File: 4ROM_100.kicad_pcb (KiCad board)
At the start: 2 copper layers, 38 x 16.6 mm, 7 parts, among them J1 Tandy_100_102_200_option_rom, J2 4ROM_prog_female, U1 SST39SF010A

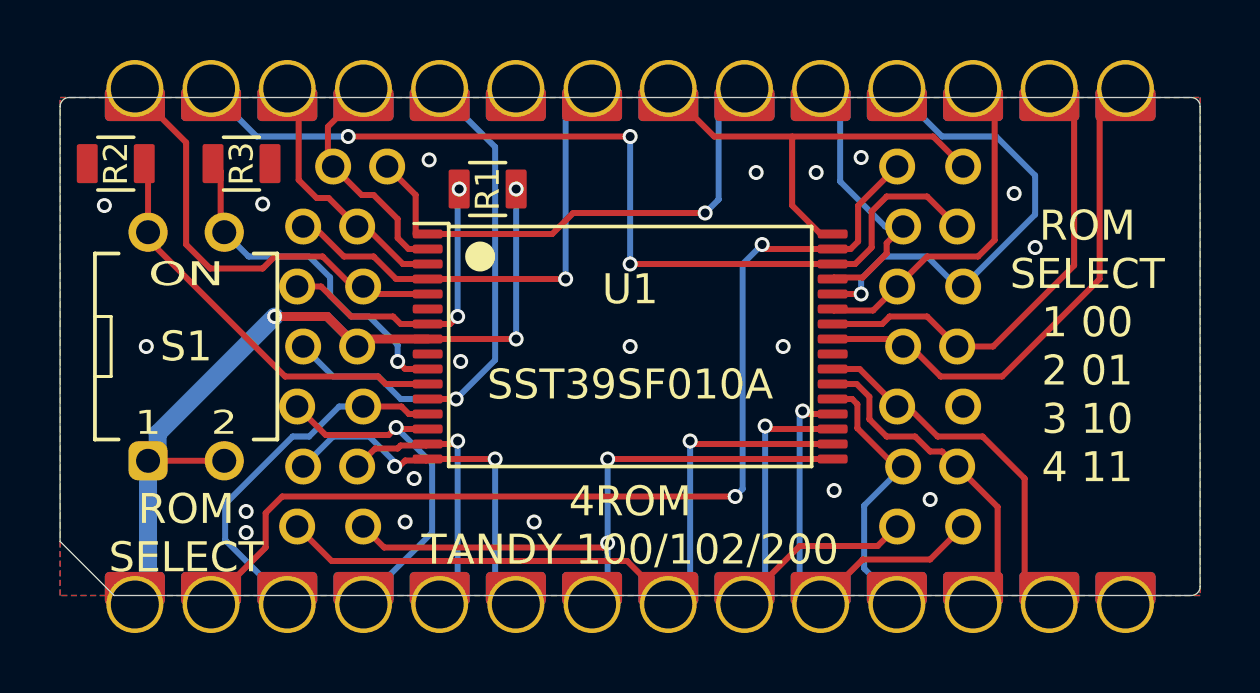
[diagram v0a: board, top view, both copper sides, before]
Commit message: 4ROM_78802 and programming adapter are now tested and verified
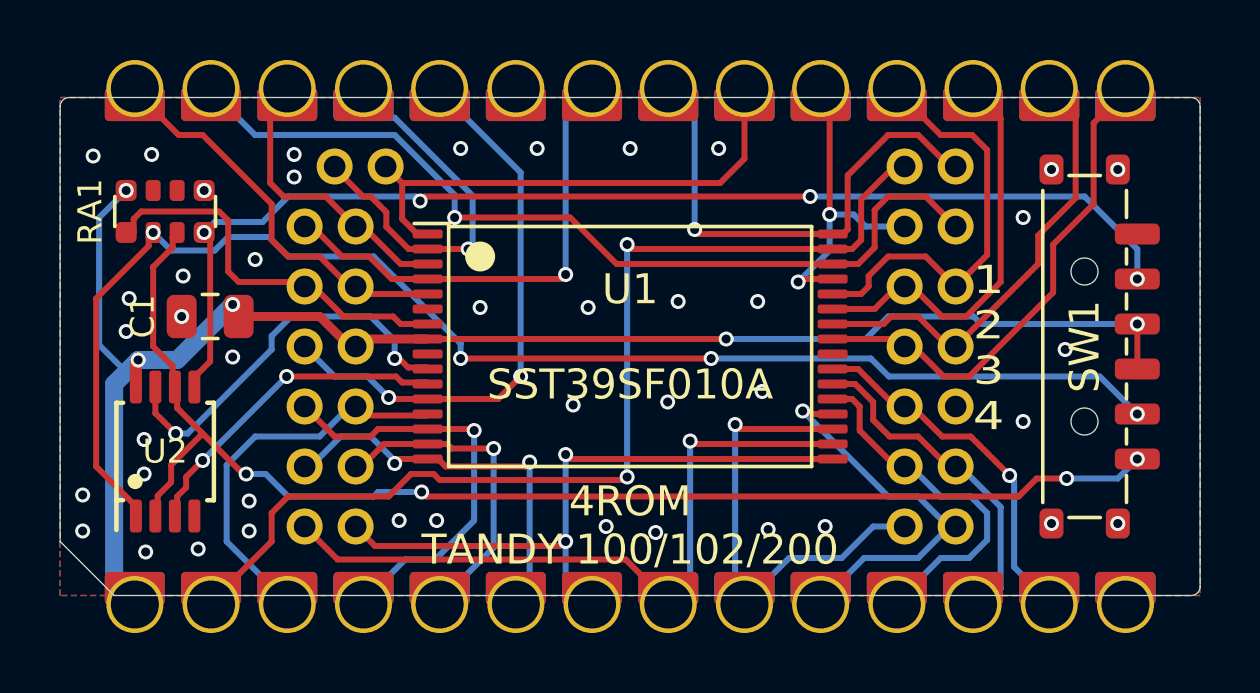
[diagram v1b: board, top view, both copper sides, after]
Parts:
- removed R1, R2, R3: 47k, 000_LOCAL:R_0805
- removed S1: DS04-254-1L-02BK, 000_LOCAL:SW_DS04-254-1L-02BK
- added C1: 0.1uF, 000_LOCAL:C_0805, F.Cu at (133.2, 98.2)
- added RA1: 100k, 000_LOCAL:R_Array_Convex_4x0612, F.Cu at (131.7, 94.7)
- added SW1: CUS-14B, 000_LOCAL:SW_SP4T_CUS-14B, F.Cu at (162.7, 99.2)
- added U2: 74LVC2G32, 000_LOCAL:TSSOP-8_3x3mm_P0.65mm, F.Cu at (131.7, 102.7)
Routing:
- net /BANK3: track 0.00 -> 46.8 mm, vias 0 -> 4
- net /BANK4: track 0.00 -> 43.8 mm, vias 0 -> 4
- net /BANK2: track 0.00 -> 38.9 mm, vias 0 -> 4
- net VCC: track 30.8 -> 53.4 mm, vias 3 -> 5
- net /A9: track 7.55 -> 12.6 mm, vias 0 -> 1
- net /~{WE}: track 10.2 -> 13.2 mm, vias 2 -> 0
- net /A15: track 13.9 -> 11.0 mm, vias 0 -> 2
- net /D0: track 9.05 -> 11.8 mm
- net /~{CE}: track 31.6 -> 29.5 mm, vias 3 -> 1
- net /D6: track 15.9 -> 13.9 mm, vias 1 -> 0
- net /~{OE}: track 14.7 -> 16.7 mm, vias 0 -> 1
- net /A6: track 11.9 -> 13.8 mm
- net /D5: track 11.6 -> 13.4 mm
- net /D7: track 9.22 -> 10.9 mm, vias 0 -> 2
- net /A14: track 14.7 -> 13.1 mm
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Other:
- board text added: "1 2 3 4"
- board text added: "C1: ${5aa54699-cac0-4512-a84c-c0ec915fe983:VALUE} RA1: 4 x 100k isolated SW1: ${a7c09382-e20a-4ce3-82c6-73f6f0e81933:VALUE} U2: ${3dfb76f3-c3d5-4850-9cfc-bf1e0ad65d1c:VALUE}"
- board text removed: "R1,R2,R3: ${00000000-0000-0000-0000-00005d22c129:VALUE} S1: ${972fe73b-6a73-4682-8533-48109a58c935:VALUE}"
- board text removed: "ROM SELECT"
- board text removed: "ROM SELECT 1 00 2 01 3 10 4 11"
